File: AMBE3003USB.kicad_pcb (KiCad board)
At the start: 2 copper layers, 72.6 x 71.6 mm, 101 parts, among them J1 McBSP, J2 ACONF, J3 CODEC, J4 USB_OTG, P1 CONFIG, U1 AMBE3003, U2 LD1117S33TR, U3 TPS3805, U4 FT232RL, U5 TPS78319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

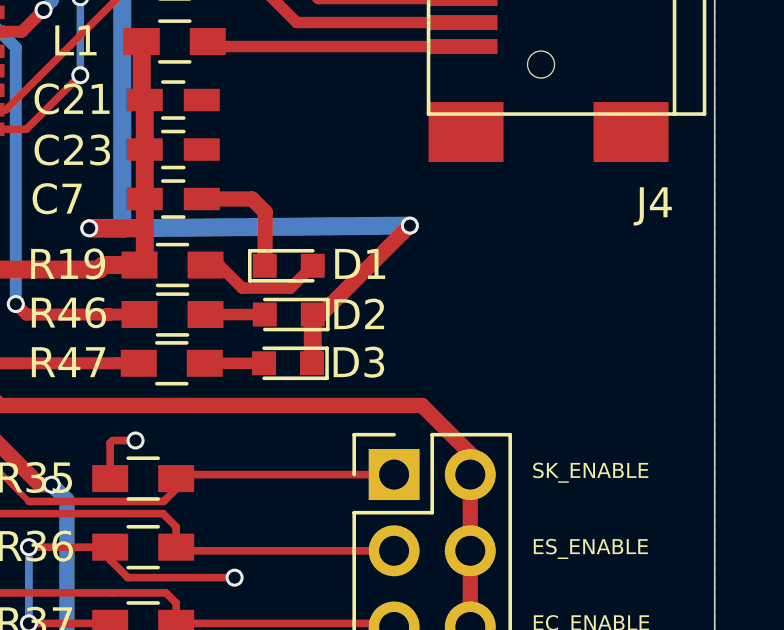
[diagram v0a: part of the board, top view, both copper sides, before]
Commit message: Add LED colors and descriptors to board
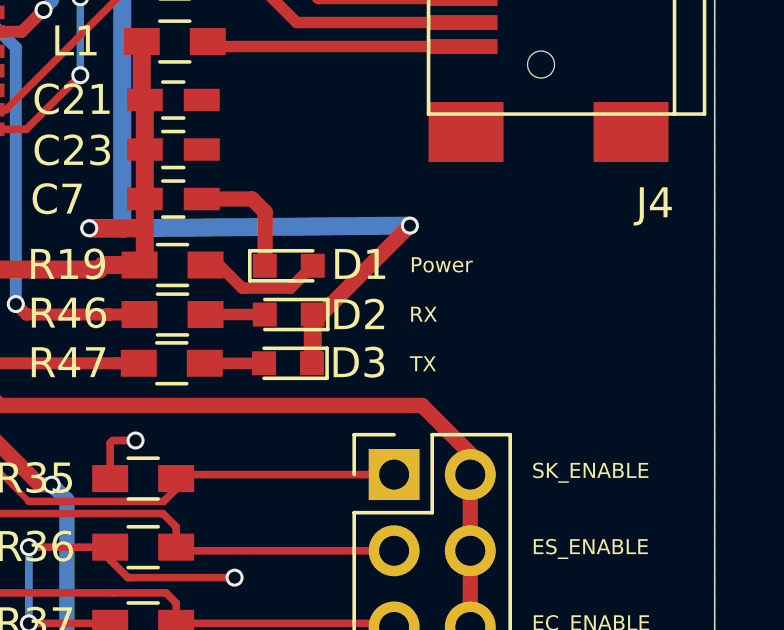
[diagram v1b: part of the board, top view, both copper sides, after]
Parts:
- D1: value LED -> green
- D2: value LED -> yellow
- D3: value LED -> red
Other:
- board text added: "Power"
- board text added: "RX"
- board text added: "TX"
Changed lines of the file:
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@@
     (area 47.726499 49.250499 120.421501 120.929501)
     (thickness 1.6)
-    (drawings 47)
+    (drawings 50)
     (tracks 1336)
     (zones 0)
@@
       (effects (font (size 1 1) (thickness 0.15)))
     )
-    (fp_text value LED (at 4.8615 -0.018) (layer F.Fab)
+    (fp_text value green (at -0.282 -0.018) (layer F.Fab)
       (effects (font (size 1 1) (thickness 0.15)))
     )
@@
       (effects (font (size 1 1) (thickness 0.15)))
     )
-    (fp_text value LED (at -4.8615 -0.008 180) (layer F.Fab)
+    (fp_text value yellow (at 0.282 -0.135 180) (layer F.Fab)
       (effects (font (size 1 1) (thickness 0.15)))
     )
@@
       (effects (font (size 1 1) (thickness 0.15)))
     )
-    (fp_text value LED (at -4.95 0.0295 180) (layer F.Fab)
+    (fp_text value red (at 0.003 -0.034 180) (layer F.Fab)
       (effects (font (size 1 1) (thickness 0.15)))
     )
@@
       (net 125 /_RUN))
   )
+  (gr_text RX (at 110.2106 73.533) (layer F.SilkS)
+    (effects (font (size 0.5 0.5) (thickness 0.1)) (justify left))
+  )
+  (gr_text TX (at 110.236 75.184) (layer F.SilkS)
+    (effects (font (size 0.5 0.5) (thickness 0.1)) (justify left))
+  )
+  (gr_text Power (at 110.236 71.882) (layer F.SilkS)
+    (effects (font (size 0.5 0.5) (thickness 0.1)) (justify left))
+  )
   (gr_text EC_ENABLE (at 114.3 83.82) (layer F.SilkS)

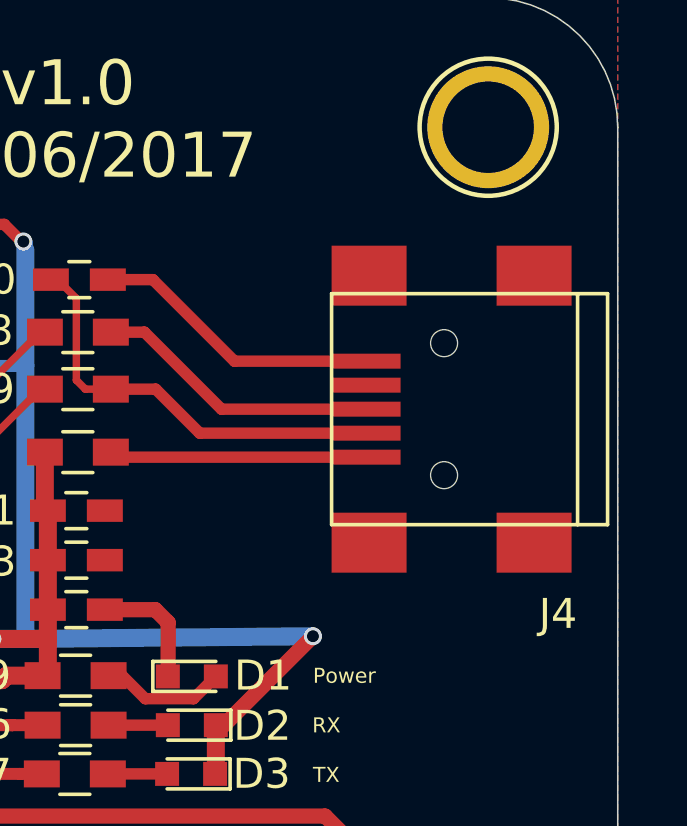
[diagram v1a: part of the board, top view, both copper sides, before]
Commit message: Change footprint of USB connector
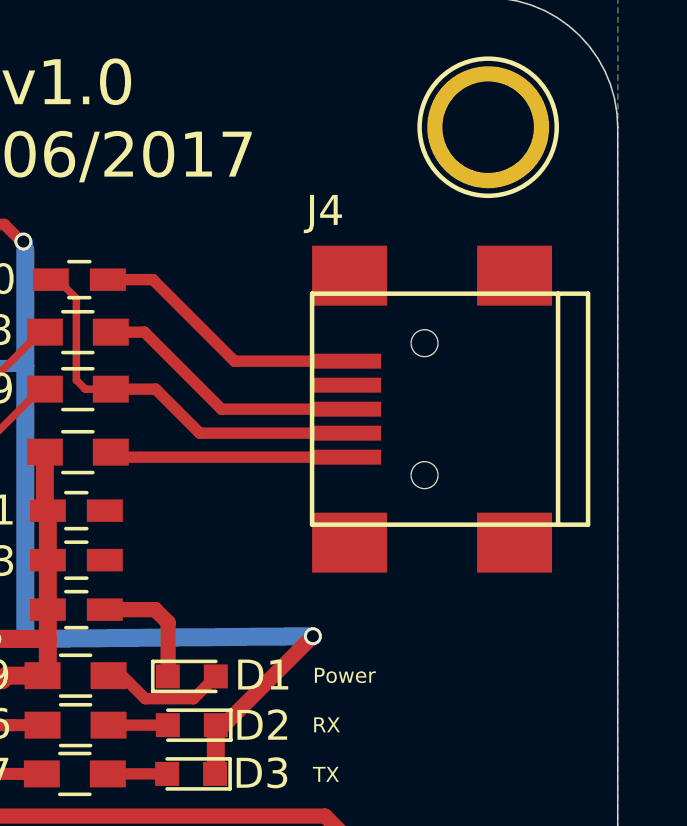
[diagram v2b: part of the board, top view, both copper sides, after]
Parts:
- J4: footprint Connectors:USB_Mini-B -> Connect:USB_Mini-B
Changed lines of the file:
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@@
     )
   )
-  (module Connectors:USB_Mini-B (layer F.Cu)
-    (at 114.808 62.992 180)
-    (descr "USB Mini-B 5-pin SMD connector")
-    (tags "USB USB_B USB_Mini connector")
-    (attr smd)
-    (fp_text reference J4 (at -3.5975 -6.829 180) (layer F.SilkS)
-      (effects (font (size 1 1) (thickness 0.15)))
-    )
-    (fp_text value USB_OTG (at -2.8355 0.156 270) (layer F.Fab)
-      (effects (font (size 1 1) (thickness 0.15)))
-    )
-    (fp_line (start -5.5 -5.7) (end 4.2 -5.7) (layer F.CrtYd) (width 0.05))
-    (fp_line (start 4.2 -5.7) (end 4.2 5.7) (layer F.CrtYd) (width 0.05))
-    (fp_line (start 4.2 5.7) (end -5.5 5.7) (layer F.CrtYd) (width 0.05))
-    (fp_line (start -5.5 5.7) (end -5.5 -5.7) (layer F.CrtYd) (width 0.05))
-    (fp_line (start -4.25 -3.85) (end -4.25 3.85) (layer F.SilkS) (width 0.12))
-    (fp_line (start -5.25 -3.85) (end -5.25 3.85) (layer F.SilkS) (width 0.12))
-    (fp_line (start -5.25 3.85) (end 3.95 3.85) (layer F.SilkS) (width 0.12))
-    (fp_line (start 3.95 3.85) (end 3.95 -3.85) (layer F.SilkS) (width 0.12))
-    (fp_line (start 3.95 -3.85) (end -5.25 -3.85) (layer F.SilkS) (width 0.12))
-    (pad 1 smd rect (at 2.8 -1.6 180) (size 2.3 0.5) (layers F.Cu F.Paste F.Mask)
-      (net 128 /VBUS))
-    (pad 2 smd rect (at 2.8 -0.8 180) (size 2.3 0.5) (layers F.Cu F.Paste F.Mask)
-      (net 127 /D-))
-    (pad 3 smd rect (at 2.8 0 180) (size 2.3 0.5) (layers F.Cu F.Paste F.Mask)
-      (net 129 /D+))
-    (pad 4 smd rect (at 2.8 0.8 180) (size 2.3 0.5) (layers F.Cu F.Paste F.Mask)
-      (net 19 "Net-(J4-Pad4)"))
-    (pad 5 smd rect (at 2.8 1.6 180) (size 2.3 0.5) (layers F.Cu F.Paste F.Mask)
-      (net 1 GND))
-    (pad 6 smd rect (at 2.7 -4.45 180) (size 2.5 2) (layers F.Cu F.Paste F.Mask)
-      (net 1 GND))
-    (pad 6 smd rect (at -2.8 -4.45 180) (size 2.5 2) (layers F.Cu F.Paste F.Mask)
-      (net 1 GND))
-    (pad 6 smd rect (at 2.7 4.45 180) (size 2.5 2) (layers F.Cu F.Paste F.Mask)
-      (net 1 GND))
-    (pad 6 smd rect (at -2.8 4.45 180) (size 2.5 2) (layers F.Cu F.Paste F.Mask)
-      (net 1 GND))
-    (pad "" np_thru_hole circle (at 0.2 -2.2 180) (size 0.9 0.9) (drill 0.9) (layers *.Cu *.Mask))
-    (pad "" np_thru_hole circle (at 0.2 2.2 180) (size 0.9 0.9) (drill 0.9) (layers *.Cu *.Mask))
-  )
   (module Inductors_SMD:L_0603_HandSoldering (layer F.Cu)
     (at 102.4 64.425 180)
@@
       (net 125 /_RUN))
   )
+  (module Connect:USB_Mini-B (layer F.Cu)
+    (at 114.808 62.992 180)
+    (descr "USB Mini-B 5-pin SMD connector")
+    (tags "USB USB_B USB_Mini connector")
+    (attr smd)
+    (fp_text reference J4 (at 4.1656 6.604 180) (layer F.SilkS)
+      (effects (font (size 1 1) (thickness 0.15)))
+    )
+    (fp_text value USB_OTG (at 0 -7.0993 180) (layer F.Fab)
+      (effects (font (size 1 1) (thickness 0.15)))
+    )
+    (fp_line (start -4.85 -5.7) (end 4.85 -5.7) (layer F.CrtYd) (width 0.05))
+    (fp_line (start 4.85 -5.7) (end 4.85 5.7) (layer F.CrtYd) (width 0.05))
+    (fp_line (start 4.85 5.7) (end -4.85 5.7) (layer F.CrtYd) (width 0.05))
+    (fp_line (start -4.85 5.7) (end -4.85 -5.7) (layer F.CrtYd) (width 0.05))
+    (fp_line (start -3.59918 -3.85064) (end -3.59918 3.85064) (layer F.SilkS) (width 0.15))
+    (fp_line (start -4.59994 -3.85064) (end -4.59994 3.85064) (layer F.SilkS) (width 0.15))
+    (fp_line (start -4.59994 3.85064) (end 4.59994 3.85064) (layer F.SilkS) (width 0.15))
+    (fp_line (start 4.59994 3.85064) (end 4.59994 -3.85064) (layer F.SilkS) (width 0.15))
+    (fp_line (start 4.59994 -3.85064) (end -4.59994 -3.85064) (layer F.SilkS) (width 0.15))
+    (pad 1 smd rect (at 3.44932 -1.6002 180) (size 2.30124 0.50038) (layers F.Cu F.Paste F.Mask)
+      (net 128 /VBUS))
+    (pad 2 smd rect (at 3.44932 -0.8001 180) (size 2.30124 0.50038) (layers F.Cu F.Paste F.Mask)
+      (net 127 /D-))
+    (pad 3 smd rect (at 3.44932 0 180) (size 2.30124 0.50038) (layers F.Cu F.Paste F.Mask)
+      (net 129 /D+))
+    (pad 4 smd rect (at 3.44932 0.8001 180) (size 2.30124 0.50038) (layers F.Cu F.Paste F.Mask)
+      (net 19 "Net-(J4-Pad4)"))
+    (pad 5 smd rect (at 3.44932 1.6002 180) (size 2.30124 0.50038) (layers F.Cu F.Paste F.Mask)
+      (net 1 GND))
+    (pad 6 smd rect (at 3.35026 -4.45008 180) (size 2.49936 1.99898) (layers F.Cu F.Paste F.Mask)
+      (net 1 GND))
+    (pad 6 smd rect (at -2.14884 -4.45008 180) (size 2.49936 1.99898) (layers F.Cu F.Paste F.Mask)
+      (net 1 GND))
+    (pad 6 smd rect (at 3.35026 4.45008 180) (size 2.49936 1.99898) (layers F.Cu F.Paste F.Mask)
+      (net 1 GND))
+    (pad 6 smd rect (at -2.14884 4.45008 180) (size 2.49936 1.99898) (layers F.Cu F.Paste F.Mask)
+      (net 1 GND))
+    (pad "" np_thru_hole circle (at 0.8509 -2.19964 180) (size 0.89916 0.89916) (drill 0.89916) (layers *.Cu *.Mask F.SilkS))
+    (pad "" np_thru_hole circle (at 0.8509 2.19964 180) (size 0.89916 0.89916) (drill 0.89916) (layers *.Cu *.Mask F.SilkS))
+  )
   (gr_text RX (at 110.2106 73.533) (layer F.SilkS)

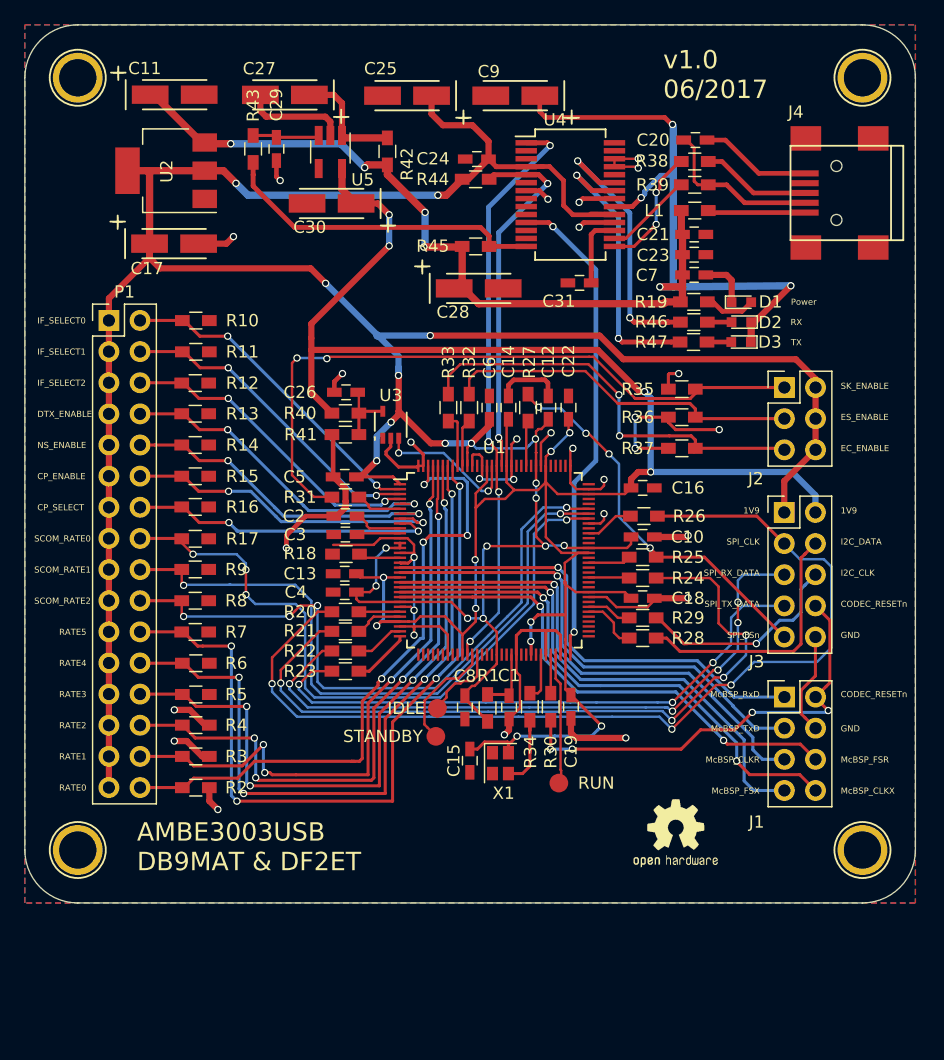
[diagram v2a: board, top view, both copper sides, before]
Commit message: Change units for caps to make BOM work
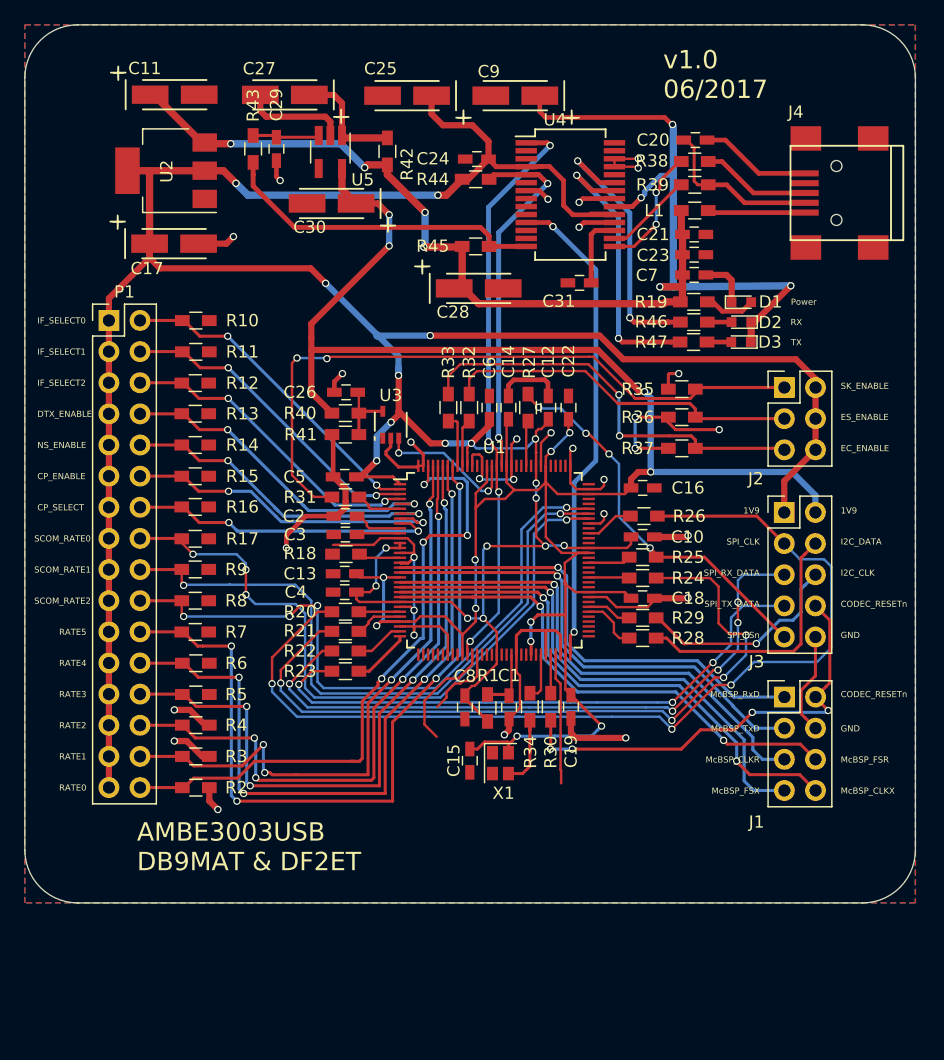
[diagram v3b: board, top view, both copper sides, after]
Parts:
- removed G***: LOGO, OPENHARDWARE:OSHWLOGO0.3IN
- removed IDLE: TP2, Measurement_Points:Measurement_Point_Round-SMD-Pad_Small
- removed REF** (x4): 1pin, Connect:1pin
- removed RUN: TP3, Measurement_Points:Measurement_Point_Round-SMD-Pad_Small
- removed STANDBY: TP1, Measurement_Points:Measurement_Point_Round-SMD-Pad_Small
- C11, C17, C2, C3: value 10µ -> 10u
- C25, C27, C28, C29: value 1µ -> 1u
- C30: value 2µ2 -> 2u2
- C9: value 4µ7 -> 4u7

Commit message: Re-add mounting holes
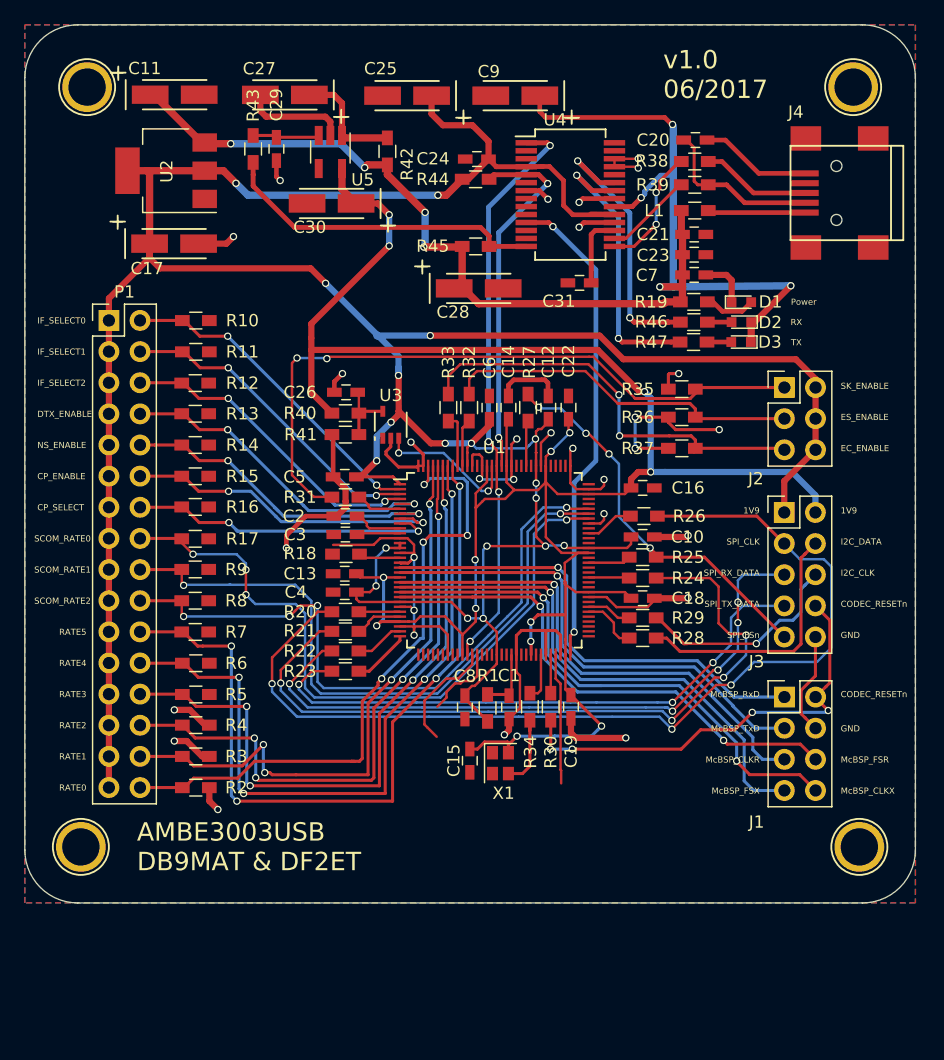
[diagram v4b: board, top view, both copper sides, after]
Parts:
- added REF**: , Connect:1pin, F.Cu at (115.3, 54.4)
- added REF**: , Connect:1pin, F.Cu at (52.8, 54.4)
- added REF**: , Connect:1pin, F.Cu at (115.8, 116.3)
- added REF**: , Connect:1pin, F.Cu at (52.3, 116.3)
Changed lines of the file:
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@@
     (tracks 1336)
     (zones 0)
-    (modules 93)
+    (modules 97)
     (nets 133)
   )
@@
     (uvia_drill 0.1)
   )
+  (module Connect:1pin (layer F.Cu)
+    (at 115.316 54.356)
+    (descr "module 1 pin (ou trou mecanique de percage)")
+    (tags DEV)
+    (fp_text reference REF** (at 0 -3.048) (layer F.SilkS) hide
+      (effects (font (size 1 1) (thickness 0.15)))
+    )
+    (fp_text value "" (at -4.318 -2.286) (layer F.Fab)
+      (effects (font (size 1 1) (thickness 0.15)))
+    )
+    (fp_circle (center 0 0) (end 0 -2.286) (layer F.SilkS) (width 0.15))
+    (pad 1 thru_hole circle (at 0 0) (size 4.064 4.064) (drill 3.048) (layers *.Cu *.Mask F.SilkS))
+  )
   (module Capacitors_Tantalum_SMD:TantalC_SizeA_EIA-3216_HandSoldering (layer F.Cu)
     (at 72.775 63.85 180)
@@
     (pad "" np_thru_hole circle (at 0.8509 2.19964 180) (size 0.89916 0.89916) (drill 0.89916) (layers *.Cu *.Mask F.SilkS))
   )
+  (module Connect:1pin (layer F.Cu)
+    (at 52.832 54.356)
+    (descr "module 1 pin (ou trou mecanique de percage)")
+    (tags DEV)
+    (fp_text reference REF** (at 0 -3.048) (layer F.SilkS) hide
+      (effects (font (size 1 1) (thickness 0.15)))
+    )
+    (fp_text value "" (at -1.778 3.302) (layer F.Fab)
+      (effects (font (size 1 1) (thickness 0.15)))
+    )
+    (fp_circle (center 0 0) (end 0 -2.286) (layer F.SilkS) (width 0.15))
+    (pad 1 thru_hole circle (at 0 0) (size 4.064 4.064) (drill 3.048) (layers *.Cu *.Mask F.SilkS))
+  )
+  (module Connect:1pin (layer F.Cu)
+    (at 115.824 116.332)
+    (descr "module 1 pin (ou trou mecanique de percage)")
+    (tags DEV)
+    (fp_text reference REF** (at 0 -3.048) (layer F.SilkS) hide
+      (effects (font (size 1 1) (thickness 0.15)))
+    )
+    (fp_text value "" (at 0 2.794) (layer F.Fab)
+      (effects (font (size 1 1) (thickness 0.15)))
+    )
+    (fp_circle (center 0 0) (end 0 -2.286) (layer F.SilkS) (width 0.15))
+    (pad 1 thru_hole circle (at 0 0) (size 4.064 4.064) (drill 3.048) (layers *.Cu *.Mask F.SilkS))
+  )
+  (module Connect:1pin (layer F.Cu)
+    (at 52.324 116.332)
+    (descr "module 1 pin (ou trou mecanique de percage)")
+    (tags DEV)
+    (fp_text reference REF** (at 0 -3.048) (layer F.SilkS) hide
+      (effects (font (size 1 1) (thickness 0.15)))
+    )
+    (fp_text value "" (at 0 2.794) (layer F.Fab)
+      (effects (font (size 1 1) (thickness 0.15)))
+    )
+    (fp_circle (center 0 0) (end 0 -2.286) (layer F.SilkS) (width 0.15))
+    (pad 1 thru_hole circle (at 0 0) (size 4.064 4.064) (drill 3.048) (layers *.Cu *.Mask F.SilkS))
+  )
   (gr_text RX (at 110.2106 73.533) (layer F.SilkS)
